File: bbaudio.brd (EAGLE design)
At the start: 88.9 x 127 mm, 38 parts, among them IC1 TLV320AIC3106, J1 AUDIO-JACKERTHENVAR, J2 AUDIO-JACKERTHENVAR, J3 AUDIO-JACKERTHENVAR, J4 AUDIO-JACKERTHENVAR, U2 V_REG_MIC2920, U3 LMZ14203, U4 VREG

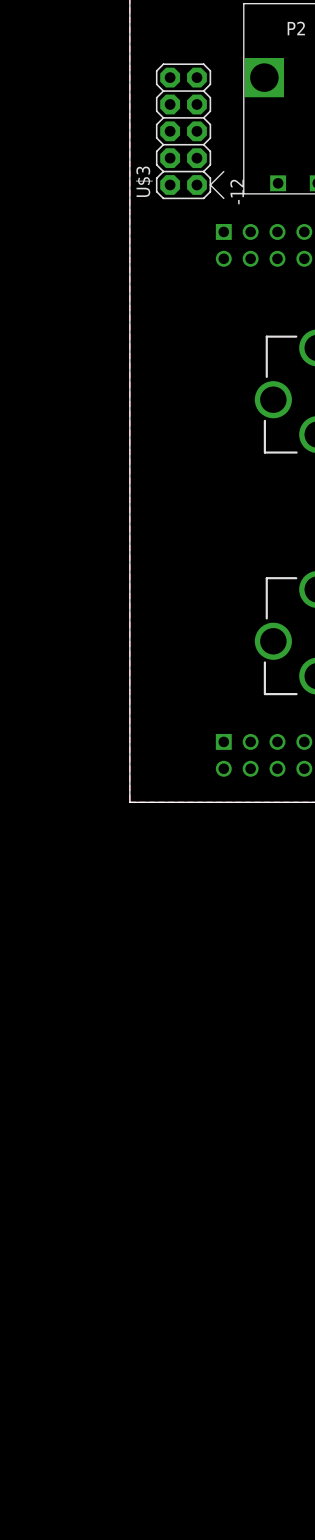
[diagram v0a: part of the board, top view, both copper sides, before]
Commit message: Started wiring up the codec
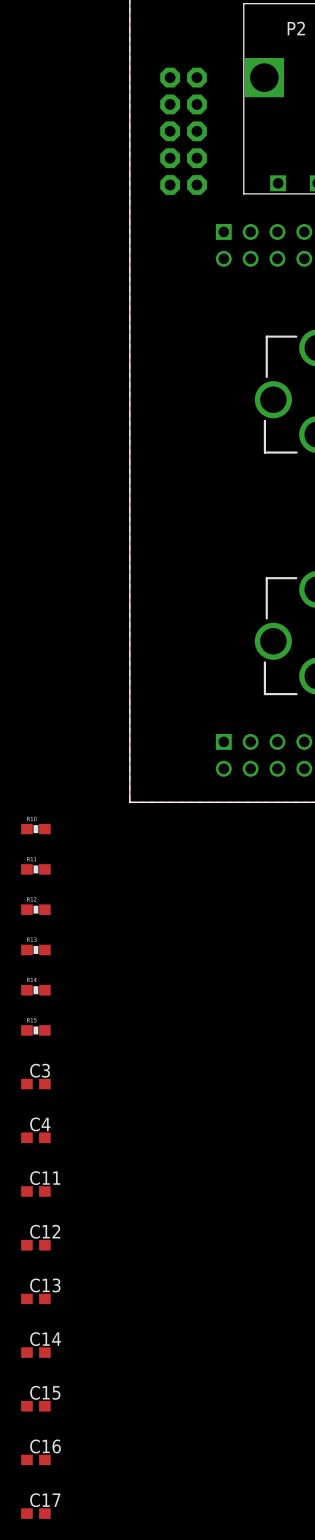
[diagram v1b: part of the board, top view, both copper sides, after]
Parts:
- added C11, C13, C15, C17: 0.1uf, rcl:C0603
- added C12, C14, C16, C4: 10uF, rcl:C0603
- added C3: 0.01uf, rcl:C0603
- added R10, R11, R12, R13, R14: 56, SparkFun-Passives:0603-RES
- added R15: 33, SparkFun-Passives:0603-RES
- flipped U$3 to the bottom, turned to 270 degrees
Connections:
- new net AUD_BCLK: IC1.39, U$1.77
- new net AUD_DIN: R11.2, R14.2, U$1.71
- new net AUD_DOUT: R12.2, R13.2, U$1.74
- new net AUD_FSK: IC1.38, U$1.75
- new net AUD_MCLK: IC1.37, R10.1, R15.2
- new net N$10: IC1.40, R11.1, R13.1
- new net N$11: IC1.41, R12.1, R14.1
- new net N$12: R15.1, U$5.P$3
- new net N$9: R10.2, U$1.87
- new net RESET: IC1.33
- new net SCL: IC1.1, U$1.63
- new net SDA: IC1.2, U$1.64
- net 1.8V: now also C10.A, C11.1, C4.1, IC1.44, U4.2; no longer C7.1, U4.3
- net 3.3V: now also C12.1, C13.1, C3.1, C7.1, IC1.36, IC1.45, IC1.46, U$5.P$4, U4.3; no longer C10.A, U4.2
- net GND: now also C11.2, C12.2, C13.2, C14.2, C15.2, C16.2, C17.2, C3.2, C4.2, IC1.15, IC1.20, IC1.21, IC1.26, IC1.42, IC1.43, U$5.P$2
- net SEL3: no longer U$1.71
- net VCC: now also C14.1, C15.1, C16.1, C17.1, IC1.16, IC1.17, IC1.24, IC1.25

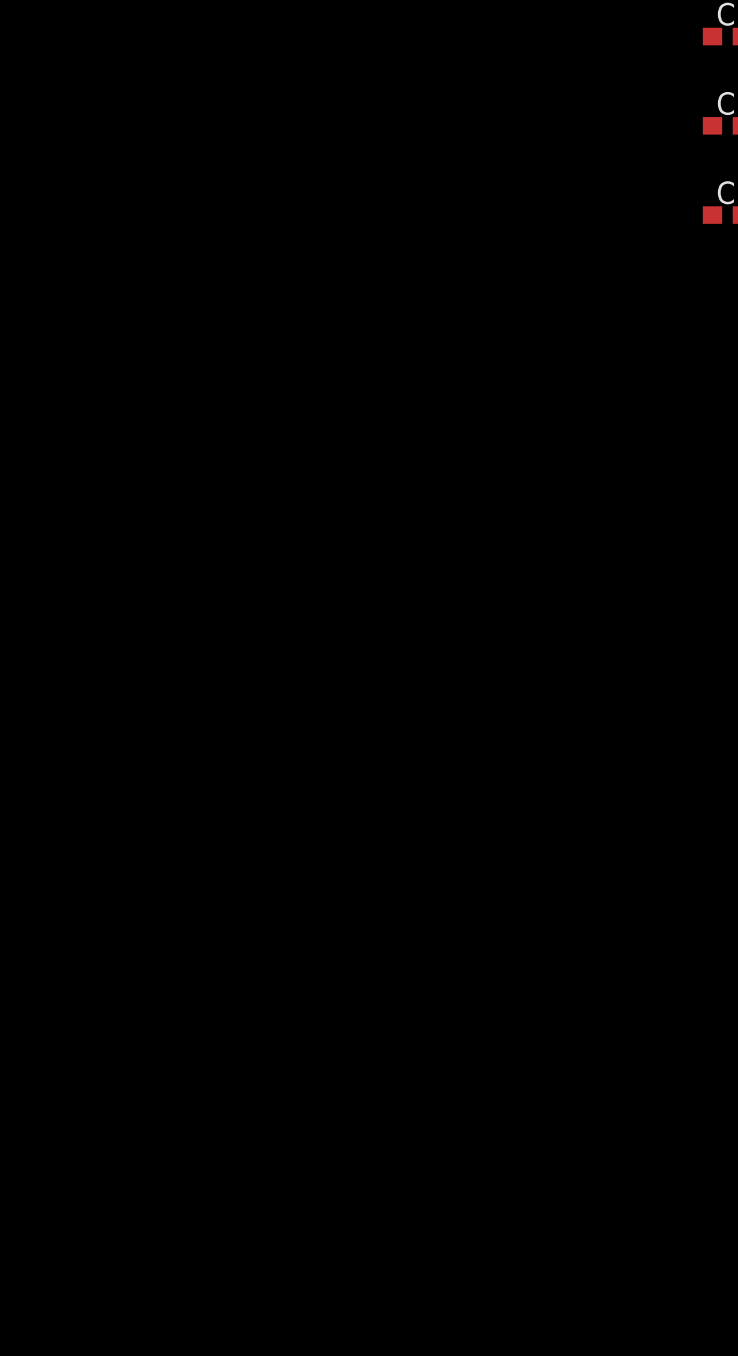
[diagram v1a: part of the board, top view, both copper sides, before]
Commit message: Added audio i/o
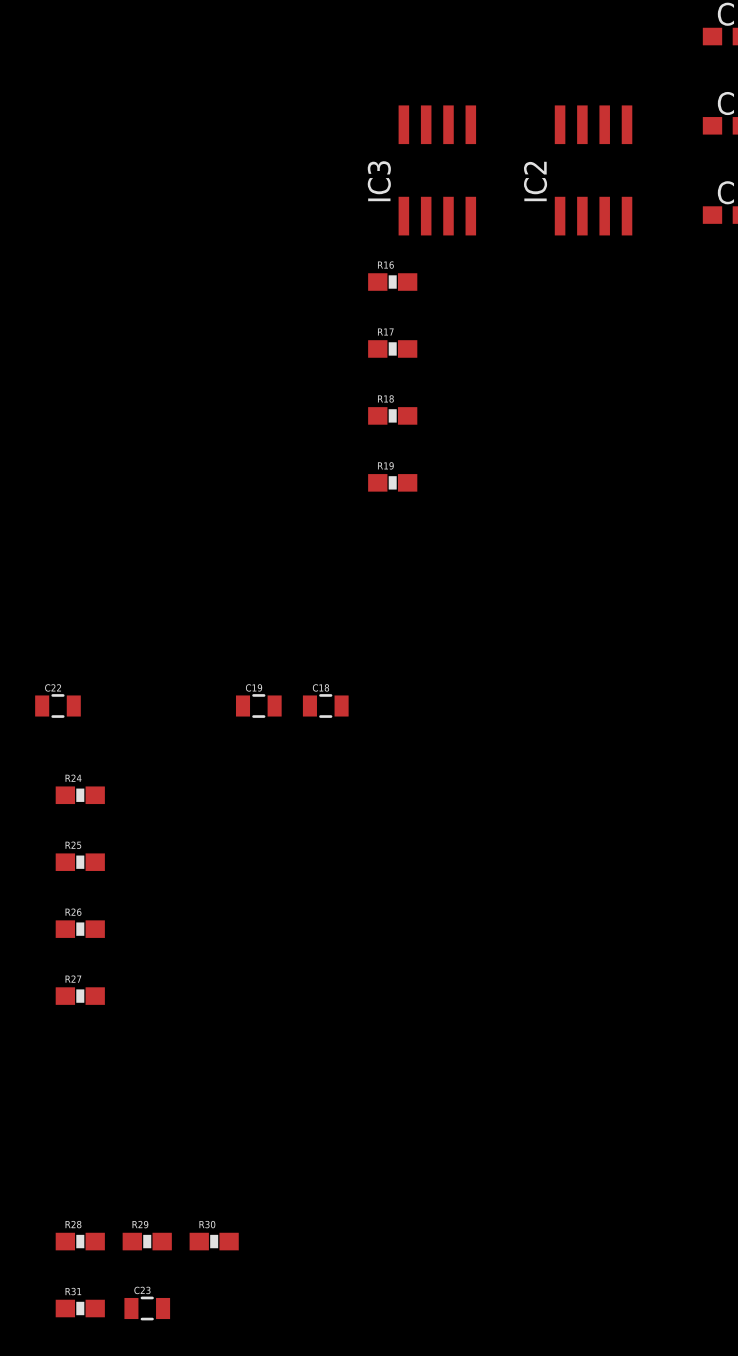
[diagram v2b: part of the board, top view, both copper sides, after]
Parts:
- added C18, C19, C22, C23: (no value), SparkFun-Passives:0805
- added IC2, IC3: LF353D, linear:SO08
- added R16, R17, R18, R19, R24, R25, R26, R27, R28, R29, R30, R31: 56, SparkFun-Passives:0603-RES
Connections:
- new net HPLCOM: IC1.19, R26.1
- new net HPLOUT: IC1.18, R25.1
- new net HPRCOM: IC1.22, R30.1
- new net HPROUT: IC1.23, R29.1
- new net LINE1LM: C19.1
- new net LINE1LP: C18.1, IC1.3
- new net LINE1RP: IC1.5
- new net N$14: IC2.1, IC2.2, R16.1
- new net N$15: C18.2, R16.2, R19.2
- new net N$16: IC2.6, IC2.7, R17.1
- new net N$17: C19.2, R17.2, R18.1
- new net N$18: IC2.3, J1.1@1, J1.1@2, J1.3
- new net N$19: IC2.5, J2.1@1, J2.1@2, J2.3
- new net N$20: C22.1, J4.1@1, J4.1@2, J4.3
- new net N$27: C22.2, IC3.1, R24.2
- new net N$28: IC3.3, R24.1, R25.2
- new net N$29: IC3.2, R26.2, R27.2
- new net N$31: C23.2, IC3.7, R28.2
- new net N$32: IC3.5, R28.1, R29.2
- new net N$33: IC3.6, R30.2, R31.2
- new net N$34: C23.1, J3.1@1, J3.1@2, J3.3
- new net V+: IC2.8, IC3.8
- new net V-: IC2.4, IC3.4
- net GND: now also IC1.4, IC1.6, J1.2, J2.2, J3.2, J4.2, R18.2, R19.1, R27.1, R31.1

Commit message: Moved some stuff around on the board
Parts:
- moved C23 202.7 mm to (77.5, 34.3), turned to 270 degrees
- moved R24 184.2 mm to (81.3, 33.0)
- moved R25 184.2 mm to (81.3, 29.2)
- moved R26 184.2 mm to (81.3, 25.4)
- moved R27 184.2 mm to (81.3, 21.6)
- moved R28 181.5 mm to (77.5, 7.62)
- moved R29 181.5 mm to (81.3, 7.62)
- moved R30 181.5 mm to (85.1, 7.62)
- moved R31 181.5 mm to (77.5, 3.81)
- moved C22 169.8 mm to (77.5, 20.3), turned to 90 degrees
- moved C19 135.9 mm to (12.7, 31.8)
- moved IC3 133.8 mm to (71.1, 27.9), turned to 180 degrees
- moved C18 127.4 mm to (12.7, 24.1), turned to 180 degrees
- moved R19 120.1 mm to (8.89, 31.8)
- moved R18 112.9 mm to (8.89, 27.9), turned to 90 degrees
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
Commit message: Re-did the audio I/O stuff
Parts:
- removed C18, C22, C23: (no value), SparkFun-Passives:0805
- removed R16: 56, SparkFun-Passives:0603-RES
- added 10K, R22: 20k, SparkFun-Passives:0603-RES
- added IC4: LF353D, linear:SO08
- added R20, R21, R23, R33: 100K, SparkFun-Passives:0603-RES
- added R32: 100k, SparkFun-Passives:0603-RES
- added R34, R35: 1K, SparkFun-Passives:0603-RES
- C19: value (none) -> 0.1uF; device SparkFun-Passives:0805 -> rcl:C0603
- R17, R19, R24, R27, R28, R29, R30, R31: value 56 -> 100K
- R18: value 56 -> 100k
- R25, R26: value 56 -> 71K
- moved C19 67.1 mm to (-8.89, -31.8)
- moved R19 49.1 mm to (-8.89, -14.0)
- moved R18 42.0 mm to (-8.89, -10.2), turned to 0 degrees
- moved R17 39.5 mm to (-8.89, -6.35), turned to 0 degrees
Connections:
- removed net LINE1LM: C19.1
- removed net N$16: IC2.6, IC2.7, R17.1
- new net AUD_REF: IC1.4, IC1.6, IC2.5, IC4.5, R20.1, R21.2
- new net MICBIAS: C19.1, IC1.13, R20.2
- new net N$21: IC4.2, R22.1, R23.2
- new net N$22: IC4.1, R22.2, R33.1
- new net N$23: IC4.6, R32.1, R33.2
- net GND: now also C19.2, IC2.3, IC4.3, R21.1; no longer IC1.4, IC1.6, R18.2, R19.1
- net LINE1LP: now also IC2.7, R18.2; no longer C18.1
- net LINE1RP: now also IC4.7, R32.2
- net N$14: now also 10K.2, R19.1; no longer IC2.2, R16.1
- net N$15: now also IC2.6, R18.1; no longer C18.2, R16.2
- net N$17: now also 10K.1, IC2.2; no longer C19.2, R18.1
- net N$18: now also R17.1; no longer IC2.3
- net N$19: now also R23.1; no longer IC2.5
- net N$20: now also R34.2; no longer C22.1
- net N$27: now also R34.1; no longer C22.2
- net N$31: now also R35.1; no longer C23.2
- net N$34: now also R35.2; no longer C23.1
- net V+: now also IC4.8
- net V-: now also IC4.4

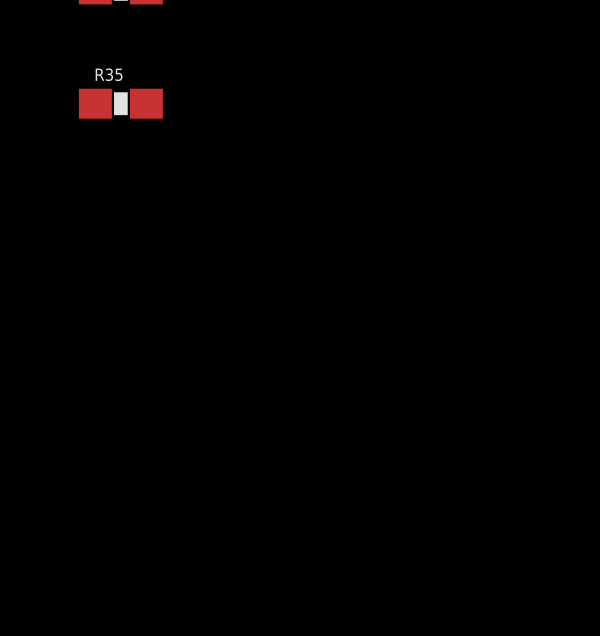
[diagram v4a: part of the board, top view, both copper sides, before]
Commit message: Add op-amp power supplies
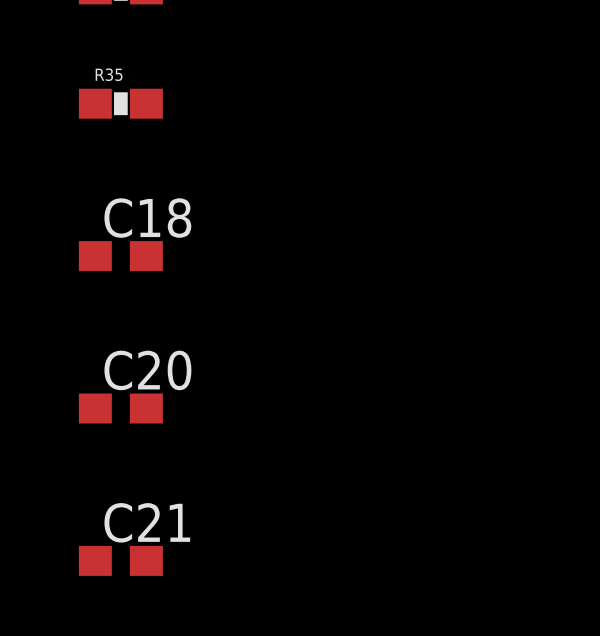
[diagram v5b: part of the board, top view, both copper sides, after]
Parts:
- added C18, C20, C21: 0.1uF, rcl:C0603
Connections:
- removed net V+: IC2.8, IC3.8, IC4.8
- removed net V-: IC2.4, IC3.4, IC4.4
- net +12V: now also C18.1, C20.1, C21.1, IC2.8, IC3.8, IC4.8
- net -12V: now also C18.2, C20.2, C21.2, IC2.4, IC3.4, IC4.4
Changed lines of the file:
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@@
 <element name="R34" library="SparkFun-Passives" package="0603-RES" value="1K" x="-8.89" y="-53.34"/>
 <element name="R35" library="SparkFun-Passives" package="0603-RES" value="1K" x="-8.89" y="-57.15"/>
+<element name="C18" library="rcl" package="C0603" value="0.1uF" x="-8.89" y="-62.23"/>
+<element name="C20" library="rcl" package="C0603" value="0.1uF" x="-8.89" y="-67.31"/>
+<element name="C21" library="rcl" package="C0603" value="0.1uF" x="-8.89" y="-72.39"/>
 </elements>
 <signals>
@@
 <contactref element="U$3" pad="10"/>
 <contactref element="U$3" pad="9"/>
+<contactref element="IC2" pad="8"/>
+<contactref element="C21" pad="1"/>
+<contactref element="IC3" pad="8"/>
+<contactref element="IC4" pad="8"/>
+<contactref element="C20" pad="1"/>
+<contactref element="C18" pad="1"/>
+<wire x1="49.95" y1="25.4" x2="73.025" y2="25.34" width="0" layer="19" extent="1-1"/>
+<wire x1="49.95" y1="27.94" x2="49.95" y2="25.4" width="0" layer="19" extent="1-1"/>
+<wire x1="50.8" y1="31.74" x2="49.95" y2="27.94" width="0" layer="19" extent="1-1"/>
 <wire x1="46.99" y1="31.62" x2="50.8" y2="31.74" width="0" layer="19" extent="1-1"/>
-<wire x1="49.95" y1="27.94" x2="50.8" y2="31.74" width="0" layer="19" extent="1-1"/>
-<wire x1="49.95" y1="25.4" x2="49.95" y2="27.94" width="0" layer="19" extent="1-1"/>
 <wire x1="40.22" y1="31.75" x2="46.99" y2="31.62" width="0" layer="19" extent="1-1"/>
 <wire x1="38.3286" y1="35.0012" x2="40.22" y2="31.75" width="0" layer="19" extent="1-1"/>
-<wire x1="6.35" y1="58.42" x2="38.3286" y2="35.0012" width="0" layer="19" extent="1-1"/>
+<wire x1="19.685" y1="26.61" x2="38.3286" y2="35.0012" width="0" layer="19" extent="1-1"/>
+<wire x1="6.35" y1="58.42" x2="19.685" y2="26.61" width="0" layer="19" extent="1-1"/>
 <wire x1="3.81" y1="58.42" x2="6.35" y2="58.42" width="0" layer="19" extent="1-1"/>
+<wire x1="-8.255" y1="-36.77" x2="19.685" y2="26.61" width="0" layer="19" extent="1-1"/>
+<wire x1="-9.74" y1="-62.23" x2="-8.255" y2="-36.77" width="0" layer="19" extent="1-1"/>
+<wire x1="-9.74" y1="-67.31" x2="-9.74" y2="-62.23" width="0" layer="19" extent="1-1"/>
+<wire x1="-9.74" y1="-72.39" x2="-9.74" y2="-67.31" width="0" layer="19" extent="1-1"/>
 </signal>
 <signal name="N$6">
@@
 <contactref element="U$3" pad="1"/>
 <contactref element="U$3" pad="2"/>
+<contactref element="IC2" pad="4"/>
+<contactref element="C21" pad="2"/>
+<contactref element="IC3" pad="4"/>
+<contactref element="IC4" pad="4"/>
+<contactref element="C18" pad="2"/>
+<contactref element="C20" pad="2"/>
+<wire x1="15.875" y1="31.81" x2="69.215" y2="30.54" width="0" layer="19" extent="1-1"/>
+<wire x1="6.35" y1="68.58" x2="15.875" y2="31.81" width="0" layer="19" extent="1-1"/>
 <wire x1="3.81" y1="68.58" x2="6.35" y2="68.58" width="0" layer="19" extent="1-1"/>
+<wire x1="-4.445" y1="-41.97" x2="15.875" y2="31.81" width="0" layer="19" extent="1-1"/>
+<wire x1="-8.04" y1="-62.23" x2="-4.445" y2="-41.97" width="0" layer="19" extent="1-1"/>
+<wire x1="-8.04" y1="-67.31" x2="-8.04" y2="-62.23" width="0" layer="19" extent="1-1"/>
+<wire x1="-8.04" y1="-72.39" x2="-8.04" y2="-67.31" width="0" layer="19" extent="1-1"/>
 </signal>
 <signal name="SCL">
@@
 <wire x1="27.11" y1="17.78" x2="27.09" y2="21.59" width="0" layer="19" extent="1-1"/>
 </signal>
-<signal name="V+">
-<contactref element="IC2" pad="8"/>
-<contactref element="IC3" pad="8"/>
-<contactref element="IC4" pad="8"/>
-<wire x1="19.685" y1="26.61" x2="73.025" y2="25.34" width="0" layer="19" extent="1-1"/>
-<wire x1="-8.255" y1="-36.77" x2="19.685" y2="26.61" width="0" layer="19" extent="1-1"/>
-</signal>
-<signal name="V-">
-<contactref element="IC2" pad="4"/>
-<contactref element="IC3" pad="4"/>
-<contactref element="IC4" pad="4"/>
-<wire x1="15.875" y1="31.81" x2="69.215" y2="30.54" width="0" layer="19" extent="1-1"/>
-<wire x1="-4.445" y1="-41.97" x2="15.875" y2="31.81" width="0" layer="19" extent="1-1"/>
-</signal>
 <signal name="N$18">

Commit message: More Schematic cleanups
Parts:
- added U$11: GND_CONNECT, sparkfun:GND_CONNECT
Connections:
- net VCC renamed VDD
- new net GNDA: C1.2, C14.2, C15.2, C16.2, C17.2, C19.2, C2.C, IC1.15, IC1.26, IC2.3, IC4.3, J1.2, J2.2, J3.2, J4.2, R21.1, R27.1, R31.1, U$11.1, U2.2
- net GND: now also U$11.2; no longer C1.2, C14.2, C15.2, C16.2, C17.2, C19.2, C2.C, IC1.15, IC1.26, IC2.3, IC4.3, J1.2, J2.2, J3.2, J4.2, R21.1, R27.1, R31.1, U2.2
